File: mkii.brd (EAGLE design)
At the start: 47.8 x 29 mm, 51 parts, among them IC1 ATMEGA32U4, Q1 16MHz, U1 GTL2003, U2 TS1117, X1 MINI-USB-32005-301

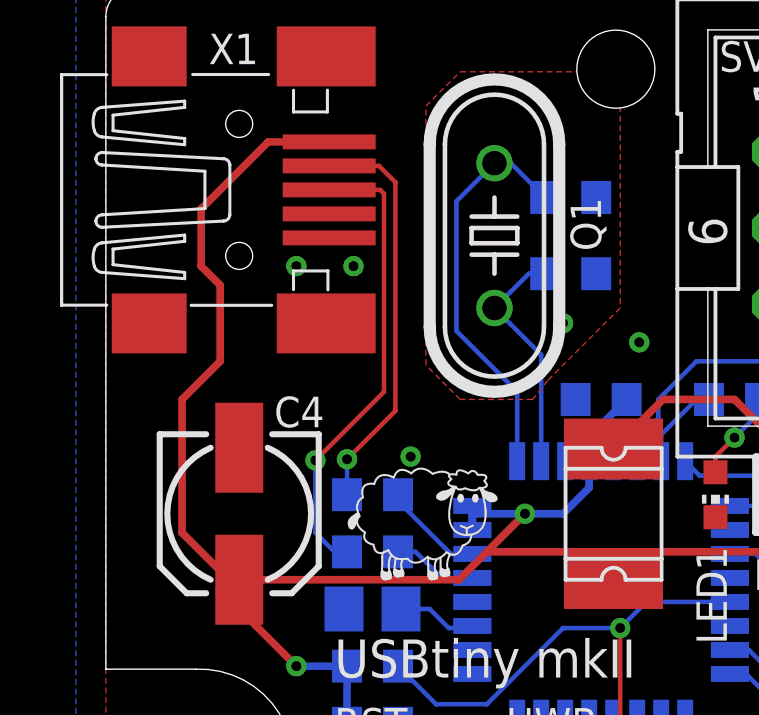
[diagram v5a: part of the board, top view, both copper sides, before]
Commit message: esd supressor for usb
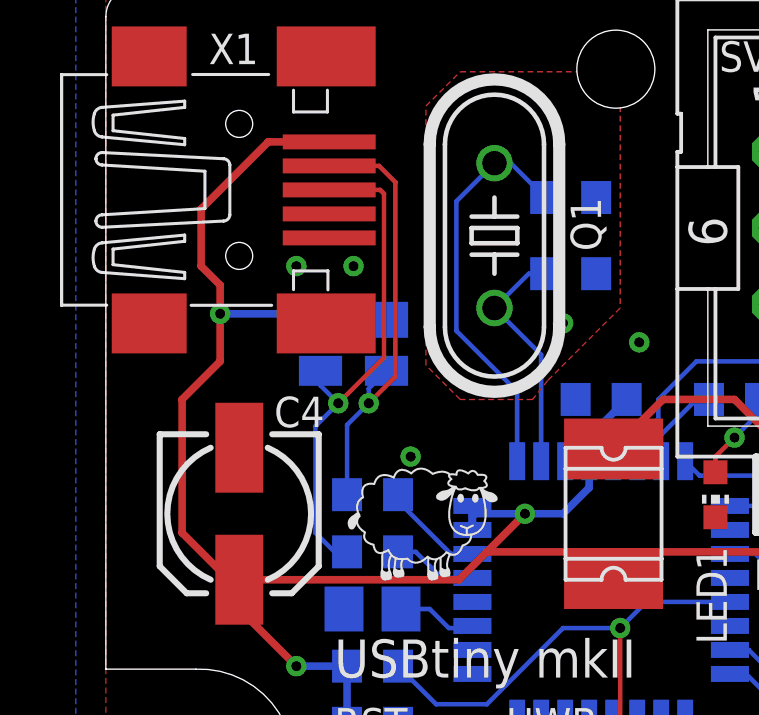
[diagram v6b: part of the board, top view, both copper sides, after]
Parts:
- added U3: PRTR5V0U2AX, nxp:SOT143B
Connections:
- removed net N$2: R5.2, X1.2
- new net N$7: R5.2, U3.2, X1.2
- net GND: now also U3.1
- net N$1: now also U3.3
- net VCC: now also U3.4
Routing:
- net N$7: track 0.00 -> 14.8 mm, vias 0 -> 1
- net N$2: track 13.5 -> 0.00 mm, vias 1 -> 0
- net VCC: track 62.3 -> 65.7 mm, vias 2 -> 3
- net N$1: track 15.4 -> 16.8 mm
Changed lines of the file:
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@@
 <layer number="19" name="Unrouted" color="6" fill="1" visible="yes" active="yes"/>
 <layer number="20" name="Dimension" color="15" fill="1" visible="yes" active="yes"/>
-<layer number="21" name="tPlace" color="7" fill="1" visible="yes" active="yes"/>
+<layer number="21" name="tPlace" color="7" fill="1" visible="no" active="yes"/>
 <layer number="22" name="bPlace" color="7" fill="1" visible="yes" active="yes"/>
-<layer number="23" name="tOrigins" color="15" fill="1" visible="yes" active="yes"/>
+<layer number="23" name="tOrigins" color="15" fill="1" visible="no" active="yes"/>
 <layer number="24" name="bOrigins" color="15" fill="1" visible="yes" active="yes"/>
 <layer number="25" name="tNames" color="7" fill="1" visible="no" active="yes"/>
-<layer number="26" name="bNames" color="7" fill="1" visible="no" active="yes"/>
+<layer number="26" name="bNames" color="7" fill="1" visible="yes" active="yes"/>
 <layer number="27" name="tValues" color="7" fill="1" visible="no" active="yes"/>
 <layer number="28" name="bValues" color="7" fill="1" visible="no" active="yes"/>
@@
 <layer number="38" name="bTest" color="7" fill="1" visible="no" active="yes"/>
 <layer number="39" name="tKeepout" color="4" fill="11" visible="no" active="yes"/>
-<layer number="40" name="bKeepout" color="1" fill="11" visible="no" active="yes"/>
+<layer number="40" name="bKeepout" color="1" fill="11" visible="yes" active="yes"/>
 <layer number="41" name="tRestrict" color="4" fill="10" visible="no" active="yes"/>
-<layer number="42" name="bRestrict" color="1" fill="10" visible="no" active="yes"/>
-<layer number="43" name="vRestrict" color="2" fill="10" visible="no" active="yes"/>
+<layer number="42" name="bRestrict" color="1" fill="10" visible="yes" active="yes"/>
+<layer number="43" name="vRestrict" color="2" fill="10" visible="yes" active="yes"/>
 <layer number="44" name="Drills" color="7" fill="1" visible="no" active="yes"/>
 <layer number="45" name="Holes" color="7" fill="1" visible="no" active="yes"/>
-<layer number="46" name="Milling" color="3" fill="1" visible="no" active="yes"/>
+<layer number="46" name="Milling" color="3" fill="1" visible="yes" active="yes"/>
 <layer number="47" name="Measures" color="7" fill="1" visible="no" active="yes"/>
 <layer number="48" name="Document" color="7" fill="1" visible="no" active="yes"/>
@@
 <element name="U$15" library="grafiken" package="PM-DOT5" value="PM-DOT5" x="31.75" y="23.495" rot="MR0"/>
 <element name="U$16" library="grafiken" package="PM-GHOSTA-5" value="PM-GHOSTA5" x="31.75" y="13.335" rot="MR0"/>
+<element name="U3" library="nxp" package="SOT143B" value="PRTR5V0U2AX" x="8.255" y="17.145" smashed="yes" rot="MR270">
+<attribute name="NAME" x="10.414" y="18.796" size="1.016" layer="26" rot="MR0"/>
+<attribute name="VALUE" x="11.43" y="19.05" size="1.27" layer="28" rot="MR270"/>
+</element>
 </elements>
 <signals>
@@
 <contactref element="R12" pad="2"/>
 <via x="45.085" y="5.715" extent="1-16" drill="0.3302"/>
+<contactref element="U3" pad="1"/>
+<contactref element="U3" pad="1"/>
 </signal>
 <signal name="VCC" class="1">
@@
 <wire x1="3.175" y1="21.59" x2="3.175" y2="19.685" width="0.254" layer="1"/>
 <wire x1="3.175" y1="19.685" x2="3.81" y2="19.05" width="0.254" layer="1"/>
-<wire x1="3.81" y1="19.05" x2="3.81" y2="16.51" width="0.254" layer="1"/>
+<wire x1="3.81" y1="18.095" x2="3.81" y2="16.51" width="0.254" layer="1"/>
 <wire x1="3.81" y1="16.51" x2="2.54" y2="15.24" width="0.254" layer="1"/>
 <wire x1="2.54" y1="15.24" x2="2.54" y2="10.795" width="0.254" layer="1"/>
@@
 <wire x1="16.923" y1="10.16" x2="12.7" y2="10.16" width="0.254" layer="1"/>
 <wire x1="16.923" y1="9.27" x2="16.923" y2="10.16" width="0.254" layer="1"/>
+<contactref element="U3" pad="4"/>
+<contactref element="U3" pad="4"/>
+<wire x1="3.81" y1="19.05" x2="3.81" y2="18.095" width="0.254" layer="1"/>
+<wire x1="3.81" y1="18.095" x2="7.155" y2="18.095" width="0.254" layer="16"/>
+<via x="3.81" y="18.095" extent="1-16" drill="0.3302"/>
 </signal>
 <signal name="XTAL2">
@@
 <wire x1="8.04" y1="10.16" x2="7.62" y2="10.16" width="0.1524" layer="16"/>
 <wire x1="7.62" y1="10.16" x2="6.985" y2="10.795" width="0.1524" layer="16"/>
-<wire x1="6.985" y1="10.795" x2="6.985" y2="13.208" width="0.1524" layer="16"/>
-<wire x1="6.985" y1="13.208" x2="9.271" y2="15.494" width="0.1524" layer="1"/>
-<wire x1="9.271" y1="15.494" x2="9.271" y2="22.098" width="0.1524" layer="1"/>
+<wire x1="9.271" y1="16.637" x2="9.271" y2="22.098" width="0.1524" layer="1"/>
 <wire x1="9.271" y1="22.098" x2="9.144" y2="22.225" width="0.1524" layer="1"/>
 <wire x1="9.144" y1="22.225" x2="7.445" y2="22.225" width="0.1524" layer="1"/>
-<via x="6.985" y="13.208" extent="1-16" drill="0.3302"/>
-</signal>
-<signal name="N$2">
-<contactref element="R5" pad="2"/>
-<contactref element="X1" pad="2"/>
-<wire x1="8.04" y1="12.065" x2="8.04" y2="13.247" width="0.1524" layer="16"/>
-<wire x1="8.04" y1="13.247" x2="9.652" y2="14.859" width="0.1524" layer="1"/>
-<wire x1="9.652" y1="14.859" x2="9.652" y2="22.479" width="0.1524" layer="1"/>
-<wire x1="7.445" y1="23.025" x2="9.106" y2="23.025" width="0.1524" layer="1"/>
-<wire x1="9.106" y1="23.025" x2="9.652" y2="22.479" width="0.1524" layer="1"/>
-<via x="8.04" y="13.247" extent="1-16" drill="0.3302"/>
+<contactref element="U3" pad="3"/>
+<wire x1="9.271" y1="16.637" x2="7.747" y2="15.113" width="0.1524" layer="1"/>
+<via x="7.747" y="15.113" extent="1-16" drill="0.3302"/>
+<wire x1="7.747" y1="15.113" x2="6.985" y2="14.351" width="0.1524" layer="16"/>
+<wire x1="6.985" y1="14.351" x2="6.985" y2="10.795" width="0.1524" layer="16"/>
+<wire x1="7.747" y1="15.113" x2="7.155" y2="15.705" width="0.1524" layer="16"/>
+<wire x1="7.155" y1="15.705" x2="7.155" y2="16.195" width="0.1524" layer="16"/>
 </signal>
 <signal name="D+">
@@
 <wire x1="20.955" y1="15.24" x2="24.13" y2="12.065" width="0.254" layer="1"/>
 </signal>
+<signal name="N$7">
+<contactref element="R5" pad="2"/>
+<contactref element="X1" pad="2"/>
+<wire x1="8.04" y1="12.065" x2="8.04" y2="14.39" width="0.1524" layer="16"/>
+<wire x1="9.652" y1="16.002" x2="9.652" y2="22.479" width="0.1524" layer="1"/>
+<wire x1="7.445" y1="23.025" x2="9.106" y2="23.025" width="0.1524" layer="1"/>
+<wire x1="9.106" y1="23.025" x2="9.652" y2="22.479" width="0.1524" layer="1"/>
+<contactref element="U3" pad="2"/>
+<wire x1="9.652" y1="16.002" x2="8.763" y2="15.113" width="0.1524" layer="1"/>
+<via x="8.763" y="15.113" extent="1-16" drill="0.3302"/>
+<wire x1="8.763" y1="15.113" x2="8.04" y2="14.39" width="0.1524" layer="16"/>
+<wire x1="9.355" y1="16.195" x2="8.763" y2="15.603" width="0.1524" layer="16"/>
+<wire x1="8.763" y1="15.603" x2="8.763" y2="15.113" width="0.1524" layer="16"/>
+</signal>
 </signals>

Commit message: growing sheep
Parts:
- U$4: value SCHAF5MM -> SCHAF7MM; device grafiken:SCHAF-5 -> grafiken:SCHAF-7
- moved U$4 0.72 mm to (7.56, 9.72)
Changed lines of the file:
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@@
 <grid distance="0.635" unitdist="mm" unit="mm" style="lines" multiple="1" display="yes" altdistance="5" altunitdist="mil" altunit="mic"/>
 <layers>
-<layer number="1" name="Top" color="4" fill="1" visible="no" active="yes"/>
+<layer number="1" name="Top" color="4" fill="1" visible="yes" active="yes"/>
 <layer number="2" name="Route2" color="1" fill="3" visible="no" active="no"/>
 <layer number="3" name="Route3" color="4" fill="3" visible="no" active="no"/>
@@
 <layer number="14" name="Route14" color="1" fill="6" visible="no" active="no"/>
 <layer number="15" name="Route15" color="4" fill="6" visible="no" active="no"/>
-<layer number="16" name="Bottom" color="1" fill="1" visible="yes" active="yes"/>
+<layer number="16" name="Bottom" color="1" fill="1" visible="no" active="yes"/>
 <layer number="17" name="Pads" color="2" fill="1" visible="yes" active="yes"/>
 <layer number="18" name="Vias" color="2" fill="1" visible="yes" active="yes"/>
 <layer number="19" name="Unrouted" color="6" fill="1" visible="yes" active="yes"/>
 <layer number="20" name="Dimension" color="15" fill="1" visible="yes" active="yes"/>
-<layer number="21" name="tPlace" color="7" fill="1" visible="no" active="yes"/>
-<layer number="22" name="bPlace" color="7" fill="1" visible="yes" active="yes"/>
-<layer number="23" name="tOrigins" color="15" fill="1" visible="no" active="yes"/>
-<layer number="24" name="bOrigins" color="15" fill="1" visible="yes" active="yes"/>
-<layer number="25" name="tNames" color="7" fill="1" visible="no" active="yes"/>
-<layer number="26" name="bNames" color="7" fill="1" visible="yes" active="yes"/>
+<layer number="21" name="tPlace" color="7" fill="1" visible="yes" active="yes"/>
+<layer number="22" name="bPlace" color="7" fill="1" visible="no" active="yes"/>
+<layer number="23" name="tOrigins" color="15" fill="1" visible="yes" active="yes"/>
+<layer number="24" name="bOrigins" color="15" fill="1" visible="no" active="yes"/>
+<layer number="25" name="tNames" color="7" fill="1" visible="yes" active="yes"/>
+<layer number="26" name="bNames" color="7" fill="1" visible="no" active="yes"/>
 <layer number="27" name="tValues" color="7" fill="1" visible="no" active="yes"/>
 <layer number="28" name="bValues" color="7" fill="1" visible="no" active="yes"/>
@@
 <layer number="37" name="tTest" color="7" fill="1" visible="no" active="yes"/>
 <layer number="38" name="bTest" color="7" fill="1" visible="no" active="yes"/>
-<layer number="39" name="tKeepout" color="4" fill="11" visible="no" active="yes"/>
-<layer number="40" name="bKeepout" color="1" fill="11" visible="yes" active="yes"/>
-<layer number="41" name="tRestrict" color="4" fill="10" visible="no" active="yes"/>
-<layer number="42" name="bRestrict" color="1" fill="10" visible="yes" active="yes"/>
+<layer number="39" name="tKeepout" color="4" fill="11" visible="yes" active="yes"/>
+<layer number="40" name="bKeepout" color="1" fill="11" visible="no" active="yes"/>
+<layer number="41" name="tRestrict" color="4" fill="10" visible="yes" active="yes"/>
+<layer number="42" name="bRestrict" color="1" fill="10" visible="no" active="yes"/>
 <layer number="43" name="vRestrict" color="2" fill="10" visible="yes" active="yes"/>
 <layer number="44" name="Drills" color="7" fill="1" visible="no" active="yes"/>
 <layer number="45" name="Holes" color="7" fill="1" visible="no" active="yes"/>
-<layer number="46" name="Milling" color="3" fill="1" visible="yes" active="yes"/>
+<layer number="46" name="Milling" color="3" fill="1" visible="no" active="yes"/>
 <layer number="47" name="Measures" color="7" fill="1" visible="no" active="yes"/>
 <layer number="48" name="Document" color="7" fill="1" visible="no" active="yes"/>
@@
 <element name="U$2" library="creative-commons" package="BY_TPLACE_HS" value="BY-TPLACE-HS" x="40.3225" y="17.9705" rot="MR0"/>
 <element name="U$3" library="creative-commons" package="SA_TPLACE_HS" value="SA-TPLACE-HALF" x="40.3225" y="12.827" rot="MR0"/>
-<element name="U$4" library="grafiken" package="SCHAF-5" value="SCHAF5MM" x="8.0645" y="9.2075"/>
+<element name="U$4" library="grafiken" package="SCHAF-7" value="SCHAF7MM" x="7.5565" y="9.7155"/>
 <element name="U$5" library="grafiken" package="PM-CHERRY-5" value="PM-CHERRY5" x="6.35" y="13.335" rot="MR0"/>
 <element name="U$6" library="grafiken" package="PM-PILL-5" value="PM-PILL5" x="11.43" y="23.495" rot="MR0"/>
@@
 </signal>
 </signals>
-<errors>
-</errors>
 </board>
 </drawing>

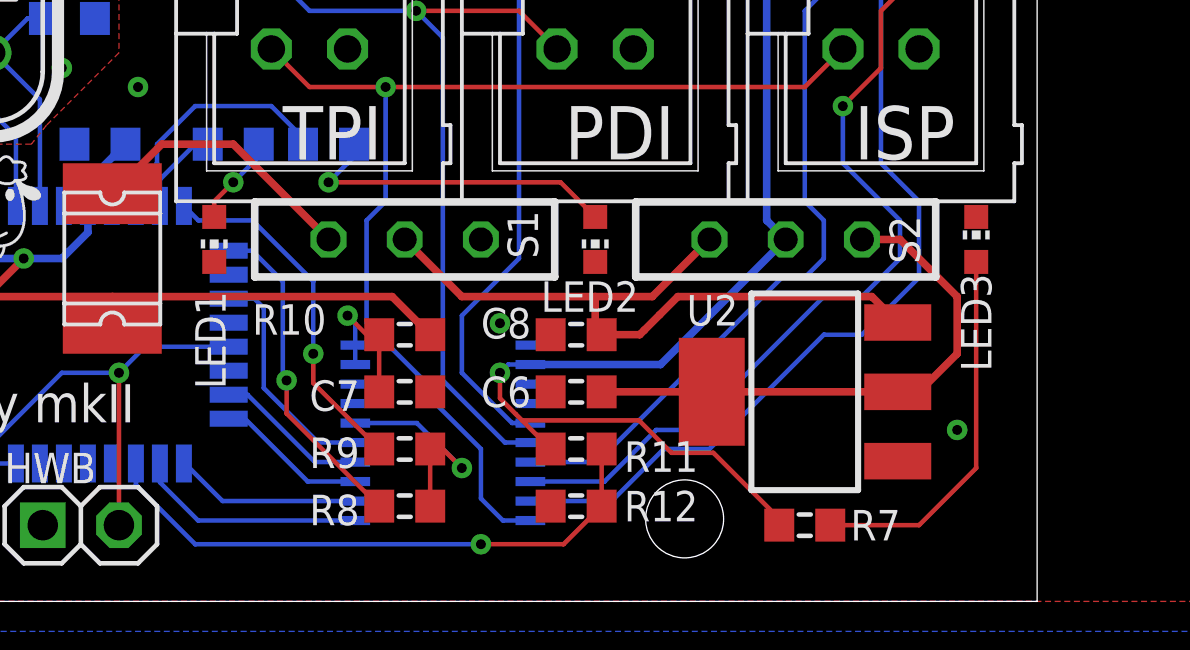
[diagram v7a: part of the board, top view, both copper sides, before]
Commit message: move leds slightly farther away from pin headers
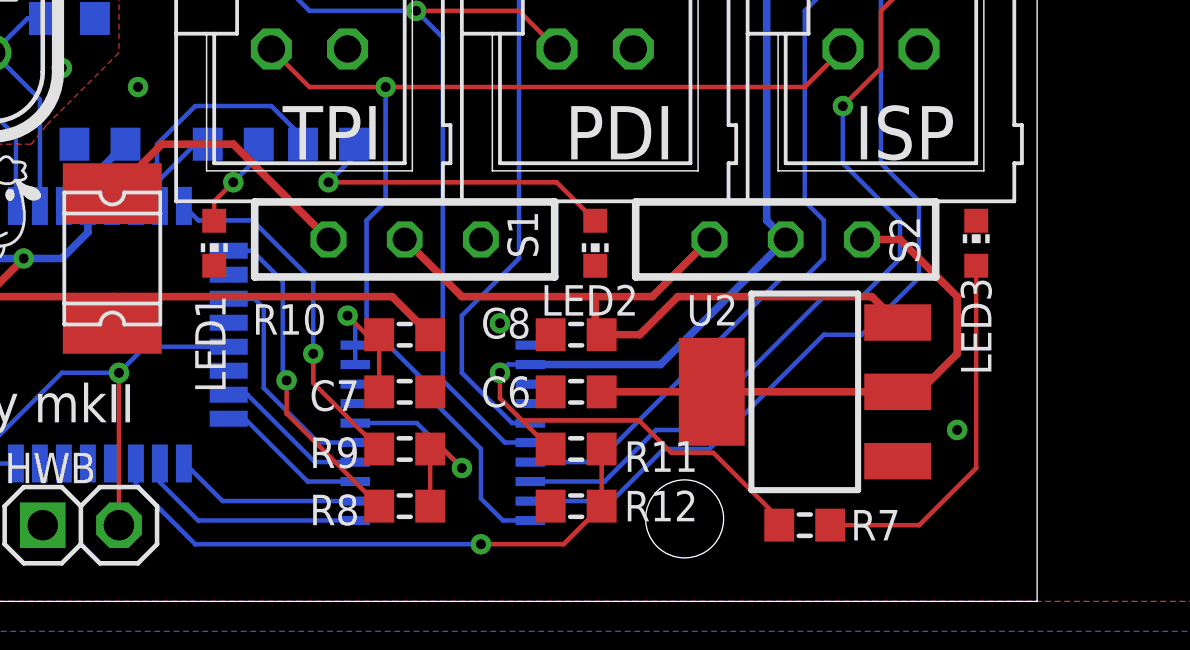
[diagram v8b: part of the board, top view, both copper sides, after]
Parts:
- moved LED1 0.13 mm to (20.3, 11.9)
- moved LED2 0.13 mm to (33.0, 11.9)
- moved LED3 0.13 mm to (45.7, 11.9)
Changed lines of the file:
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@@
 <attribute name="VALUE" x="24.765" y="13.335" size="1.27" layer="28" rot="MR0"/>
 </element>
-<element name="LED1" library="led" package="CHIP-LED0603" value="" x="20.32" y="12.065" smashed="yes" rot="R180">
-<attribute name="NAME" x="20.701" y="7.08" size="1.016" layer="25" rot="R90"/>
-<attribute name="VALUE" x="18.415" y="13.716" size="1.27" layer="27" ratio="10" rot="R180"/>
-</element>
-<element name="LED2" library="led" package="CHIP-LED0603" value="" x="33.02" y="12.065" smashed="yes" rot="R180">
-<attribute name="NAME" x="31.21" y="9.652" size="1.016" layer="25"/>
-<attribute name="VALUE" x="31.115" y="13.716" size="1.27" layer="27" ratio="10" rot="R180"/>
+<element name="LED1" library="led" package="CHIP-LED0603" value="" x="20.32" y="11.938" smashed="yes" rot="R180">
+<attribute name="NAME" x="20.701" y="6.953" size="1.016" layer="25" rot="R90"/>
+<attribute name="VALUE" x="18.415" y="13.589" size="1.27" layer="27" ratio="10" rot="R180"/>
+</element>
+<element name="LED2" library="led" package="CHIP-LED0603" value="" x="33.02" y="11.938" smashed="yes" rot="R180">
+<attribute name="NAME" x="31.21" y="9.525" size="1.016" layer="25"/>
+<attribute name="VALUE" x="31.115" y="13.589" size="1.27" layer="27" ratio="10" rot="R180"/>
 </element>
 <element name="R4" library="rcl" package="R0603" value="22" x="8.89" y="10.16" smashed="yes" rot="MR0">
@@
 <attribute name="VALUE" x="40.64" y="4.445" size="1.27" layer="27" rot="R180"/>
 </element>
-<element name="LED3" library="led" package="CHIP-LED0603" value="" x="45.72" y="12.065" smashed="yes">
-<attribute name="NAME" x="45.212" y="10.922" size="1.016" layer="25" rot="R270"/>
-<attribute name="VALUE" x="47.625" y="10.414" size="1.27" layer="27" ratio="10"/>
+<element name="LED3" library="led" package="CHIP-LED0603" value="" x="45.72" y="11.938" smashed="yes">
+<attribute name="NAME" x="45.212" y="10.795" size="1.016" layer="25" rot="R270"/>
+<attribute name="VALUE" x="47.625" y="10.287" size="1.27" layer="27" ratio="10"/>
 </element>
 <element name="SV1" library="con-ml" package="ML6" value="ISP" x="42.545" y="20.955" smashed="yes" rot="R270">
@@
 <via x="20.955" y="13.97" extent="1-16" drill="0.3302"/>
 <wire x1="20.955" y1="13.97" x2="20.32" y2="13.335" width="0.1524" layer="1"/>
-<wire x1="20.32" y1="13.335" x2="20.32" y2="12.815" width="0.1524" layer="1"/>
+<wire x1="20.32" y1="13.335" x2="20.32" y2="12.688" width="0.1524" layer="1"/>
 </signal>
 <signal name="N$13">
@@
 <wire x1="24.98" y1="14.82" x2="24.13" y2="13.97" width="0.1524" layer="16"/>
 <via x="24.13" y="13.97" extent="1-16" drill="0.3302"/>
-<wire x1="24.13" y1="13.97" x2="31.865" y2="13.97" width="0.1524" layer="1"/>
-<wire x1="31.865" y1="13.97" x2="33.02" y2="12.815" width="0.1524" layer="1"/>
+<wire x1="24.13" y1="13.97" x2="31.738" y2="13.97" width="0.1524" layer="1"/>
+<wire x1="31.738" y1="13.97" x2="33.02" y2="12.688" width="0.1524" layer="1"/>
 </signal>
 <signal name="N$1">
@@
 <contactref element="R7" pad="1"/>
 <contactref element="LED3" pad="A"/>
-<wire x1="45.72" y1="11.315" x2="45.72" y2="4.445" width="0.1524" layer="1"/>
+<wire x1="45.72" y1="11.188" x2="45.72" y2="4.445" width="0.1524" layer="1"/>
 <wire x1="45.72" y1="4.445" x2="43.815" y2="2.54" width="0.1524" layer="1"/>
 <wire x1="43.815" y1="2.54" x2="40.855" y2="2.54" width="0.1524" layer="1"/>
@@
 </signal>
 </signals>
+<errors>
+</errors>
 </board>
 </drawing>
